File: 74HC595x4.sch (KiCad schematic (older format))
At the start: 1 part, among them P1 CONN_01X06

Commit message: расставлено по сетке, исправлены ошибки
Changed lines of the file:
@@
 LIBS:contrib
 LIBS:valves
+LIBS:74HC595x4-cache
 EELAYER 25 0
 EELAYER END
@@
 	5400 3150 4650 3150
 Wire Wire Line
-	4650 1850 4650 5550
-Connection ~ 4650 1850
-Wire Wire Line
 	4650 4350 5400 4350
 Connection ~ 4650 3150
@@
 Wire Wire Line
 	4450 5650 5400 5650
-Wire Wire Line
-	4450 1950 4450 5650
-Connection ~ 4450 1950
 Wire Wire Line
 	5400 3250 4450 3250
@@
 	3800 1750 3800 1400
 Connection ~ 3350 1750
+Wire Wire Line
+	4450 5650 4450 2050
+Connection ~ 4450 2050
+Wire Wire Line
+	4650 5550 4650 1950
+Connection ~ 4650 1950
 $EndSCHEMATC

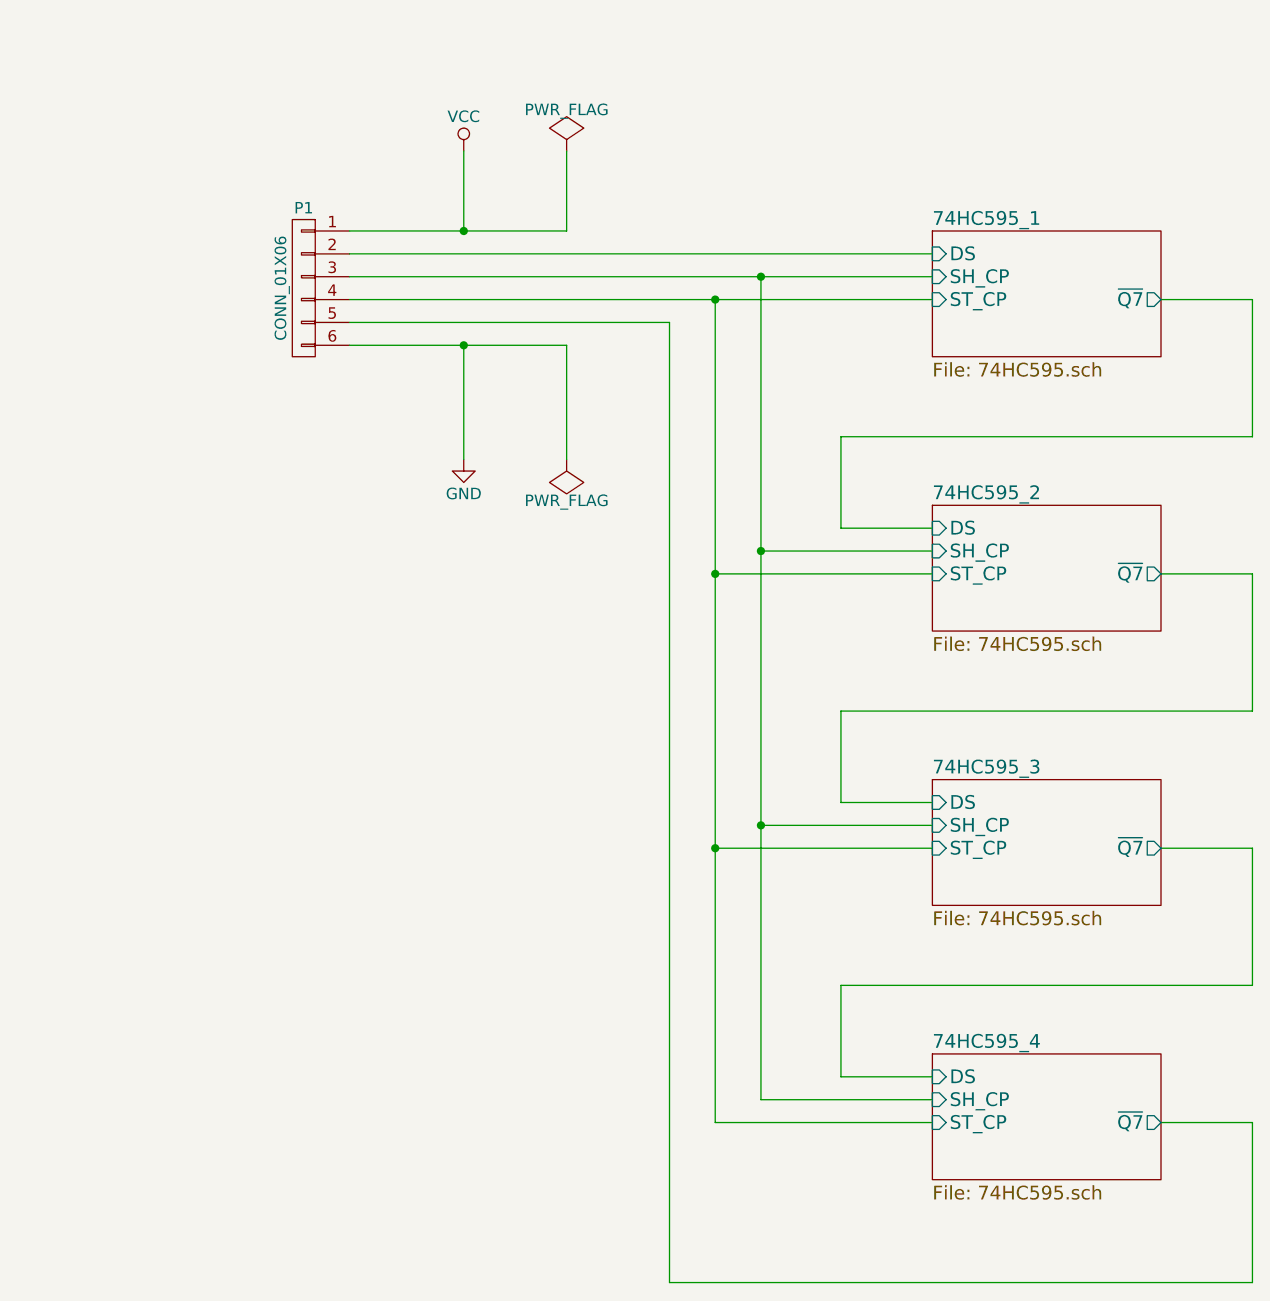
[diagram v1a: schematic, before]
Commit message: изменен входной разъем
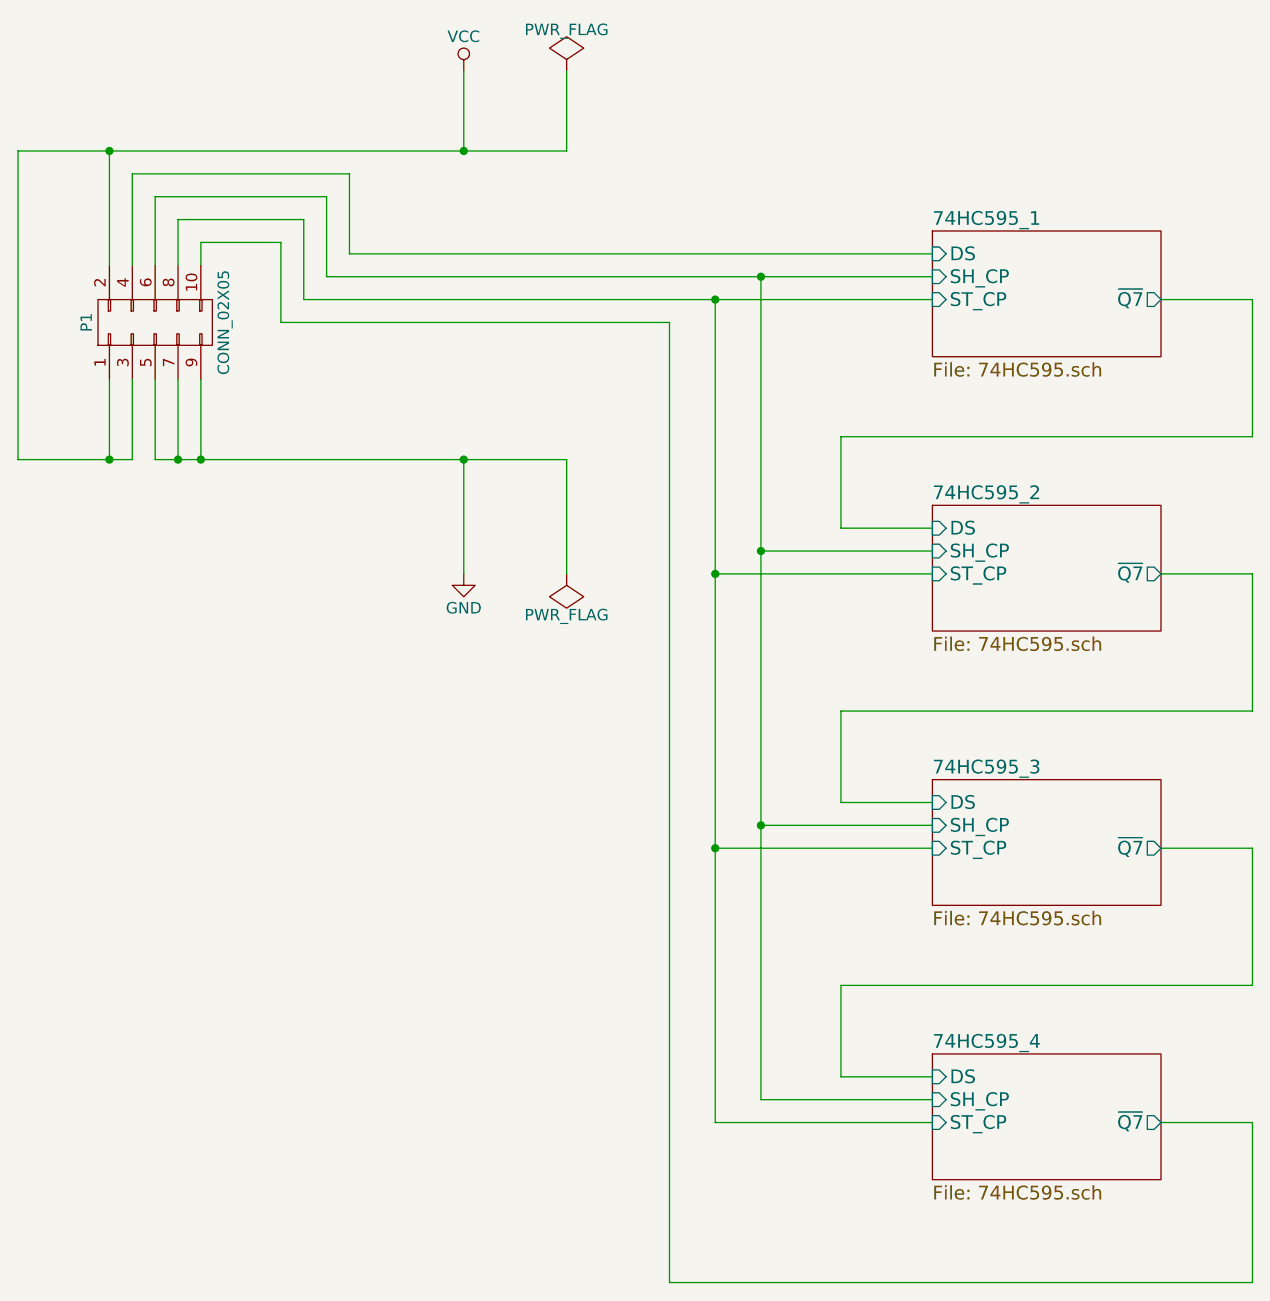
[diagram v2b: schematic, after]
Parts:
- removed P1: CONN_01X06, Pin_Headers:Pin_Header_Straight_1x06, symbol CONN_01X06
- added P1: CONN_02X05, Connect:IDC_Header_Straight_10pins, symbol CONN_02X05
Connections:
- net 74HC595_1/DS: now also P1.4 (P4)
- net 74HC595_1/SH_CP: now also P1.6 (P6)
- net 74HC595_1/ST_CP: now also P1.8 (P8)
- net 74HC595_4/~Q7: now also P1.10 (P10)
- net GND: now also P1.5 (P5), P1.7 (P7), P1.9 (P9)
- net VCC: now also P1.1 (P1), P1.2 (P2), P1.3 (P3)
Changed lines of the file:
@@
 Wire Wire Line
 	5000 4250 5400 4250
-$Comp
-L CONN_01X06 P1
-U 1 1 57D782AD
-P 2650 2000
-F 0 "P1" H 2650 2350 50  0000 C CNN
-F 1 "CONN_01X06" V 2750 2000 50  0000 C CNN
-F 2 "Pin_Headers:Pin_Header_Straight_1x06" H 2650 2000 50  0001 C CNN
-F 3 "" H 2650 2000 50  0000 C CNN
-	1    2650 2000
-	-1   0    0    -1
-$EndComp
 Wire Wire Line
 	2850 1850 5400 1850
 Wire Wire Line
-	2850 1950 5400 1950
+	2750 1950 5400 1950
 Wire Wire Line
-	5400 2050 2850 2050
+	2650 2050 5400 2050
 Wire Wire Line
 	6800 5650 6800 6350
@@
 Connection ~ 4450 3250
 Wire Wire Line
-	5400 4450 4450 4450
+	4450 4450 5400 4450
 Connection ~ 4450 4450
 Wire Wire Line
@@
 L GND #PWR01
 U 1 1 57D79F5E
-P 3350 2750
-F 0 "#PWR01" H 3350 2500 50  0001 C CNN
-F 1 "GND" H 3350 2600 50  0000 C CNN
-F 2 "" H 3350 2750 50  0000 C CNN
-F 3 "" H 3350 2750 50  0000 C CNN
-	1    3350 2750
+P 3350 3250
+F 0 "#PWR01" H 3350 3000 50  0001 C CNN
+F 1 "GND" H 3350 3100 50  0000 C CNN
+F 2 "" H 3350 3250 50  0000 C CNN
+F 3 "" H 3350 3250 50  0000 C CNN
+	1    3350 3250
 	1    0    0    -1
 $EndComp
@@
 L VCC #PWR02
 U 1 1 57D79FD4
-P 3350 1400
-F 0 "#PWR02" H 3350 1250 50  0001 C CNN
-F 1 "VCC" H 3350 1550 50  0000 C CNN
-F 2 "" H 3350 1400 50  0000 C CNN
-F 3 "" H 3350 1400 50  0000 C CNN
-	1    3350 1400
+P 3350 1050
+F 0 "#PWR02" H 3350 900 50  0001 C CNN
+F 1 "VCC" H 3350 1200 50  0000 C CNN
+F 2 "" H 3350 1050 50  0000 C CNN
+F 3 "" H 3350 1050 50  0000 C CNN
+	1    3350 1050
 	1    0    0    -1
 $EndComp
 Wire Wire Line
-	3350 1400 3350 1750
+	3350 1400 3350 1050
 Wire Wire Line
-	2850 1750 3800 1750
+	1400 1400 3800 1400
 Wire Wire Line
-	3350 2750 3350 2250
+	3350 3250 3350 2750
 Wire Wire Line
-	2850 2250 3800 2250
-Wire Wire Line
-	4250 2150 2850 2150
+	4250 2150 2550 2150
 Wire Wire Line
 	6800 3250 6400 3250
@@
 L PWR_FLAG #FLG03
 U 1 1 57D7E0DA
-P 3800 1400
-F 0 "#FLG03" H 3800 1495 50  0001 C CNN
-F 1 "PWR_FLAG" H 3800 1580 50  0000 C CNN
-F 2 "" H 3800 1400 50  0000 C CNN
-F 3 "" H 3800 1400 50  0000 C CNN
-	1    3800 1400
+P 3800 1050
+F 0 "#FLG03" H 3800 1145 50  0001 C CNN
+F 1 "PWR_FLAG" H 3800 1230 50  0000 C CNN
+F 2 "" H 3800 1050 50  0000 C CNN
+F 3 "" H 3800 1050 50  0000 C CNN
+	1    3800 1050
 	1    0    0    -1
 $EndComp
@@
 L PWR_FLAG #FLG04
 U 1 1 57D7E4C2
-P 3800 2750
-F 0 "#FLG04" H 3800 2845 50  0001 C CNN
-F 1 "PWR_FLAG" H 3800 2930 50  0000 C CNN
-F 2 "" H 3800 2750 50  0000 C CNN
-F 3 "" H 3800 2750 50  0000 C CNN
-	1    3800 2750
+P 3800 3250
+F 0 "#FLG04" H 3800 3345 50  0001 C CNN
+F 1 "PWR_FLAG" H 3800 3430 50  0000 C CNN
+F 2 "" H 3800 3250 50  0000 C CNN
+F 3 "" H 3800 3250 50  0000 C CNN
+	1    3800 3250
 	-1   0    0    1
 $EndComp
 Wire Wire Line
-	3800 2250 3800 2750
-Connection ~ 3350 2250
+	3800 2750 3800 3250
+Connection ~ 3350 2750
 Wire Wire Line
-	3800 1750 3800 1400
-Connection ~ 3350 1750
+	3800 1400 3800 1050
+Connection ~ 3350 1400
 Wire Wire Line
-	4450 5650 4450 2050
+	4450 2050 4450 5650
 Connection ~ 4450 2050
 Wire Wire Line
-	4650 5550 4650 1950
+	4650 1950 4650 5550
 Connection ~ 4650 1950
+$Comp
+L CONN_02X05 P1
+U 1 1 583B1DE3
+P 2000 2150
+F 0 "P1" H 2000 2450 50  0000 C CNN
+F 1 "CONN_02X05" H 2000 1850 50  0000 C CNN
+F 2 "Connect:IDC_Header_Straight_10pins" H 2000 950 50  0001 C CNN
+F 3 "" H 2000 950 50  0000 C CNN
+	1    2000 2150
+	0    -1   -1   0
+$EndComp
+Wire Wire Line
+	1800 1900 1800 1400
+Wire Wire Line
+	1900 1500 2850 1500
+Wire Wire Line
+	2850 1500 2850 1850
+Wire Wire Line
+	2000 1600 2750 1600
+Wire Wire Line
+	2750 1600 2750 1950
+Wire Wire Line
+	1400 1400 1400 2750
+Connection ~ 1800 1400
+Wire Wire Line
+	1800 2400 1800 2750
+Connection ~ 1800 2750
+Wire Wire Line
+	1900 2750 1900 2400
+Wire Wire Line
+	1400 2750 1900 2750
+Wire Wire Line
+	1900 1500 1900 1900
+Wire Wire Line
+	2000 1600 2000 1900
+Wire Wire Line
+	2650 2050 2650 1700
+Wire Wire Line
+	2650 1700 2100 1700
+Wire Wire Line
+	2100 1700 2100 1900
+Wire Wire Line
+	2550 2150 2550 1800
+Wire Wire Line
+	2550 1800 2200 1800
+Wire Wire Line
+	2200 1800 2200 1900
+Wire Wire Line
+	2000 2400 2000 2750
+Wire Wire Line
+	2000 2750 3800 2750
+Wire Wire Line
+	2200 2750 2200 2400
+Wire Wire Line
+	2100 2400 2100 2750
+Connection ~ 2100 2750
+Connection ~ 2200 2750
 $EndSCHEMATC
